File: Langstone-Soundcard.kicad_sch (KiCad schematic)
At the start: 27 parts, among them J1 NF_IN, J2 USB, J3 NF_OUT, SW1 HID, U1 PCM2902, Y1 12MHz

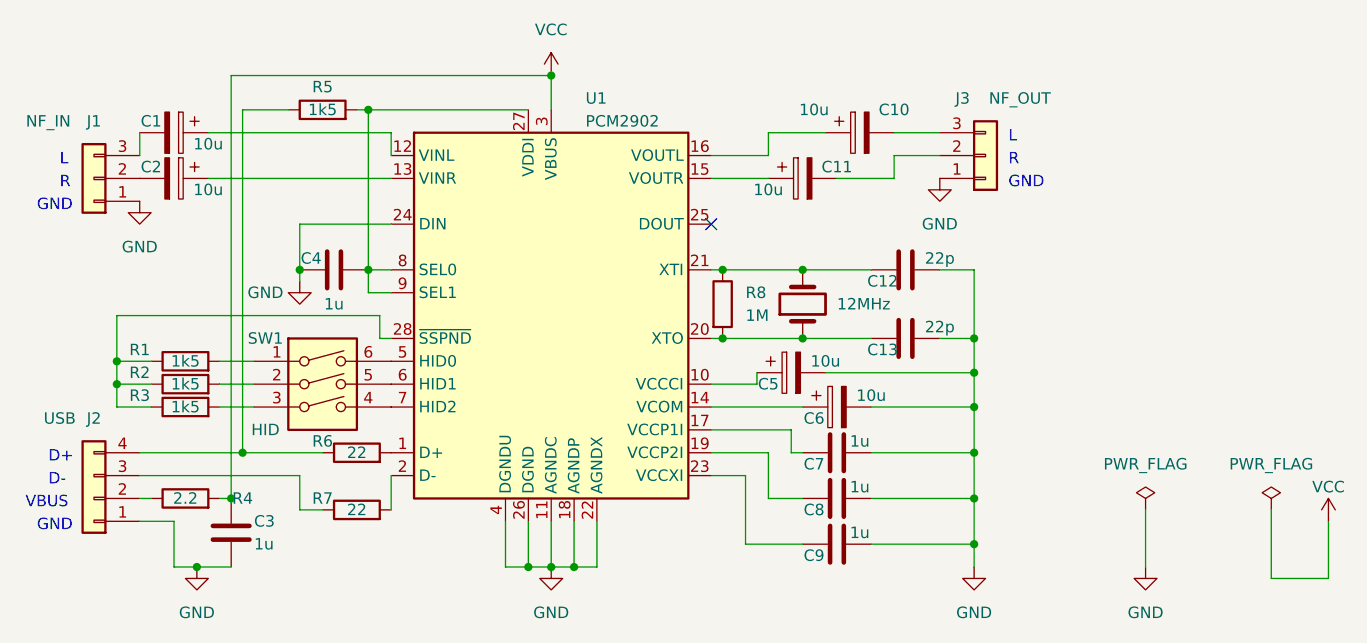
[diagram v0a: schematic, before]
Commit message: 22pF auf 10pF geändert, Footprints auf SMD0805 geändert, SMD Quartz, SMD-Pin Regler auf SMD geändert. Stecker auf PH2.0 geändert.
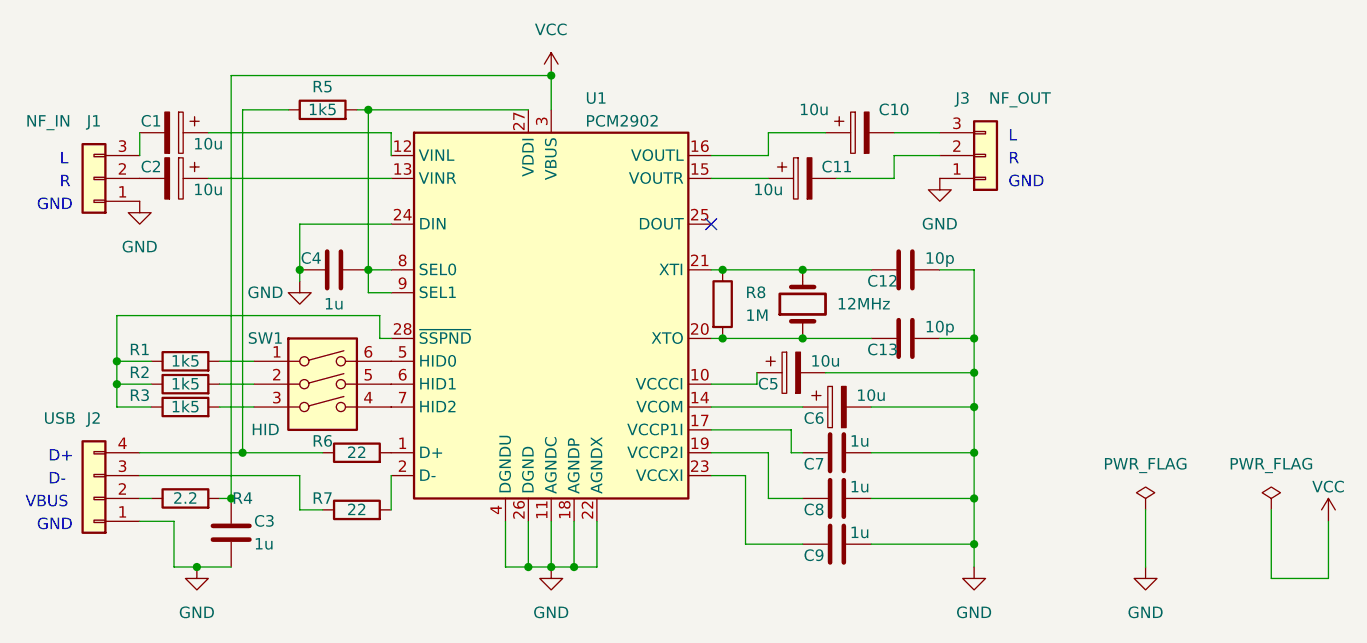
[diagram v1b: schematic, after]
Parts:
- C12, C13: value 22p -> 10p; footprint Capacitor_SMD:C_1206_3216Metric_Pad1.33x1.80mm_HandSolder -> Capacitor_SMD:C_0805_2012Metric_Pad1.18x1.45mm_HandSolder
- C3, C4, C7, C8, C9: footprint Capacitor_SMD:C_1206_3216Metric_Pad1.33x1.80mm_HandSolder -> Capacitor_SMD:C_0805_2012Metric_Pad1.18x1.45mm_HandSolder
- J1, J3: footprint Connector_JST:JST_XH_B3B-XH-A_1x03_P2.50mm_Vertical -> Connector_JST:JST_PH_B3B-PH-K_1x03_P2.00mm_Vertical
- J2: footprint Connector_JST:JST_XH_B4B-XH-A_1x04_P2.50mm_Vertical -> Connector_JST:JST_PH_B4B-PH-K_1x04_P2.00mm_Vertical
- R1, R2, R3, R4, R5, R6, R7, R8: footprint Resistor_SMD:R_1206_3216Metric_Pad1.30x1.75mm_HandSolder -> Resistor_SMD:R_0805_2012Metric_Pad1.20x1.40mm_HandSolder
- SW1: footprint Button_Switch_THT:SW_DIP_SPSTx03_Slide_9.78x9.8mm_W7.62mm_P2.54mm -> Button_Switch_SMD:SW_DIP_SPSTx03_Slide_KingTek_DSHP03TJ_W5.25mm_P1.27mm_JPin
- Y1: footprint Crystal:Crystal_SMD_HC49-SD_HandSoldering -> Crystal:Crystal_SMD_G8-2Pin_3.2x1.5mm_HandSoldering
